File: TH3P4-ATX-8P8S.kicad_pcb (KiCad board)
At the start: 2 copper layers, 18.2 x 23.2 mm, 2 parts, among them J1 ATX_8pin_female_solder, J2 ATX_8pin_male

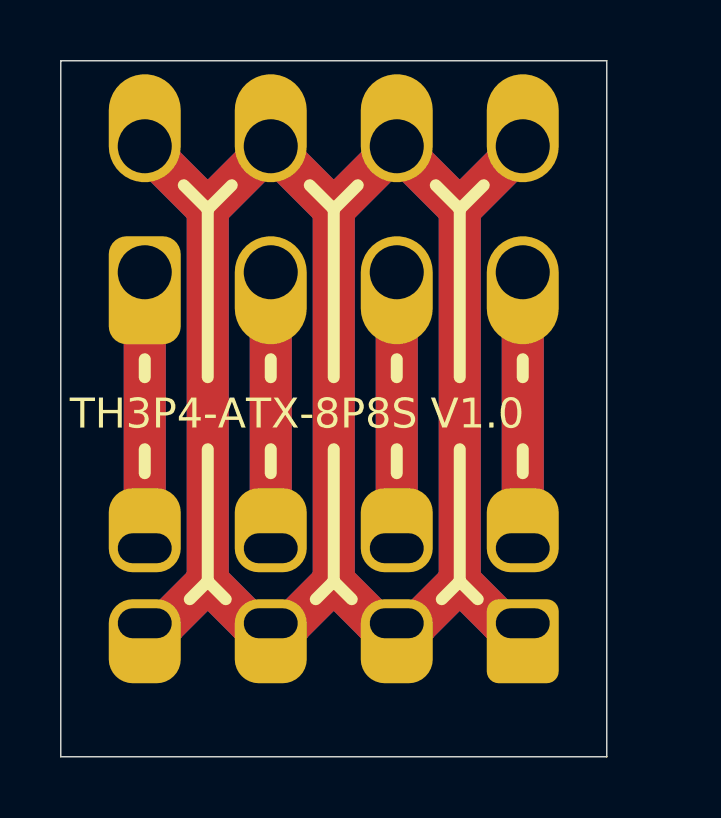
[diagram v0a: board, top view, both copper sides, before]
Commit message: Updated with real life experiences
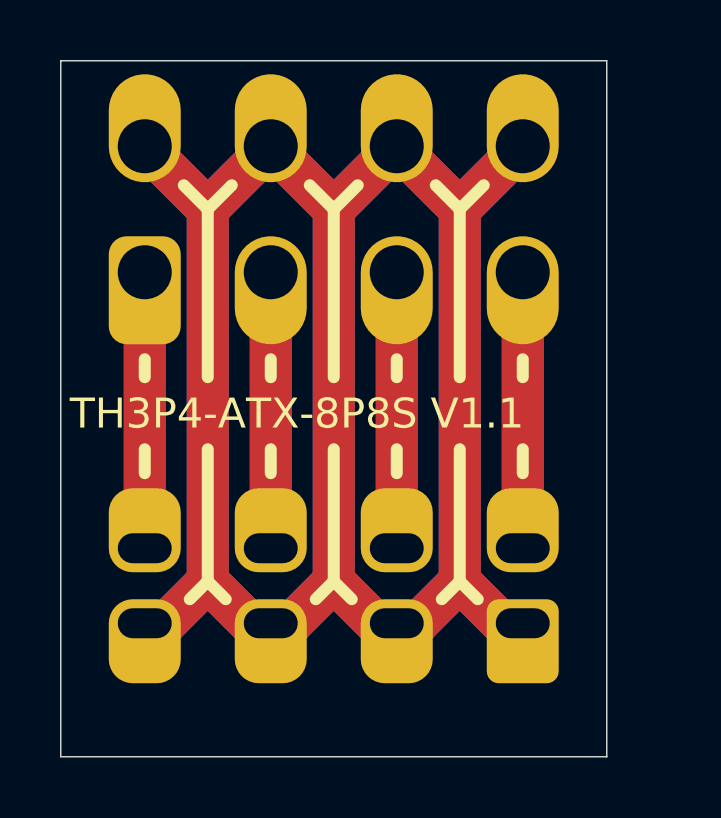
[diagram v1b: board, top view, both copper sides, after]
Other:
- board text added: "TH3P4-ATX-8P8S V1.1"
- board text removed: "TH3P4-ATX-8P8S V1.0"
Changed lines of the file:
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@@
 				(font
 					(size 1 1)
-					(thickness 0.1)
+					(thickness 0.15)
 				)
 				(justify mirror)
@@
 				(font
 					(size 1 1)
-					(thickness 0.1)
+					(thickness 0.15)
 				)
 				(justify left mirror)
@@
 		(end 158.1 94.25)
 		(stroke
-			(width 0.1)
+			(width 0.15)
 			(type default)
 		)
@@
 		(end 158.1 92.65)
 		(stroke
-			(width 0.1)
+			(width 0.15)
 			(type default)
 		)
@@
 			(font
 				(size 1 1)
-				(thickness 0.1)
+				(thickness 0.15)
 			)
 			(justify left bottom mirror)
@@
 			(font
 				(size 1 1)
-				(thickness 0.1)
+				(thickness 0.15)
 			)
 			(justify bottom mirror)
 		)
 	)
-	(gr_text "TH3P4-ATX-8P8S V1.0"
+	(gr_text "TH3P4-ATX-8P8S V1.1"
 		(at 141.2 95 0)
 		(layer "F.SilkS")
@@
 			(font
 				(size 1 1)
-				(thickness 0.1)
+				(thickness 0.15)
 			)
 			(justify left bottom)
